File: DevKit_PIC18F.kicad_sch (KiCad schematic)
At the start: 29 parts, among them J1 PIC_ICSP_ICD, J2 USB_B, J3 5P_UART, J4 RA_PORT, J5 RB_PORT, J6 RD_PORT, J7 RC_PORT, J8 RE_PORT, SW1 SW_RST, X1 16MHz

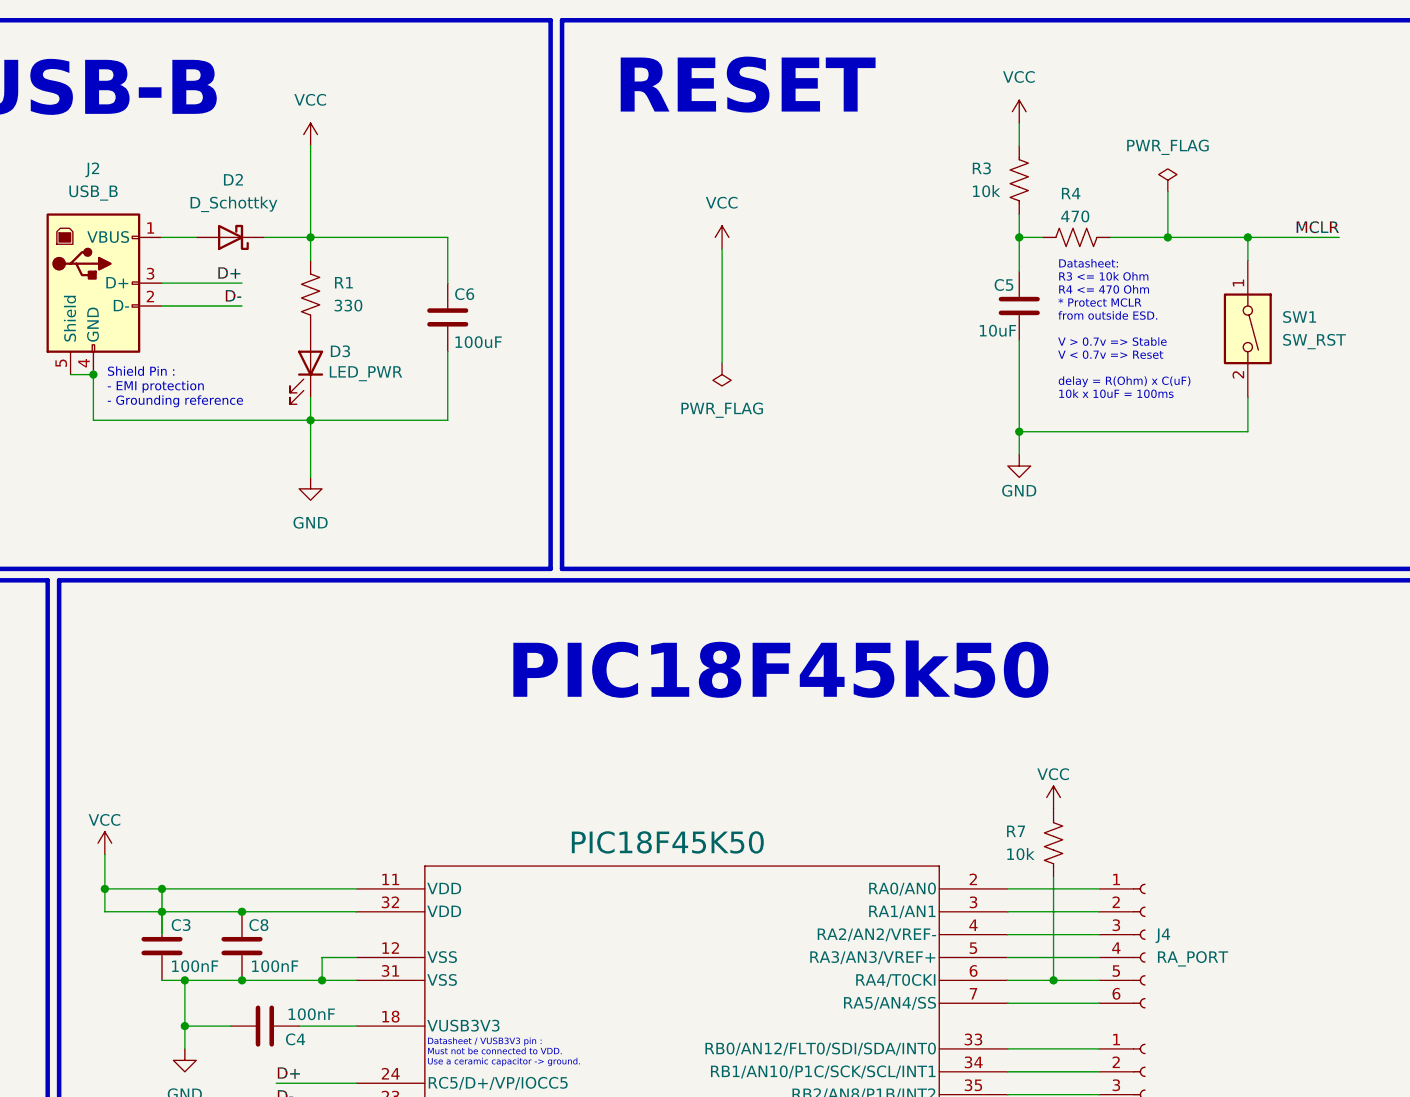
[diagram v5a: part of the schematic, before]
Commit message: Fix PWR_Flag & GND on PCB
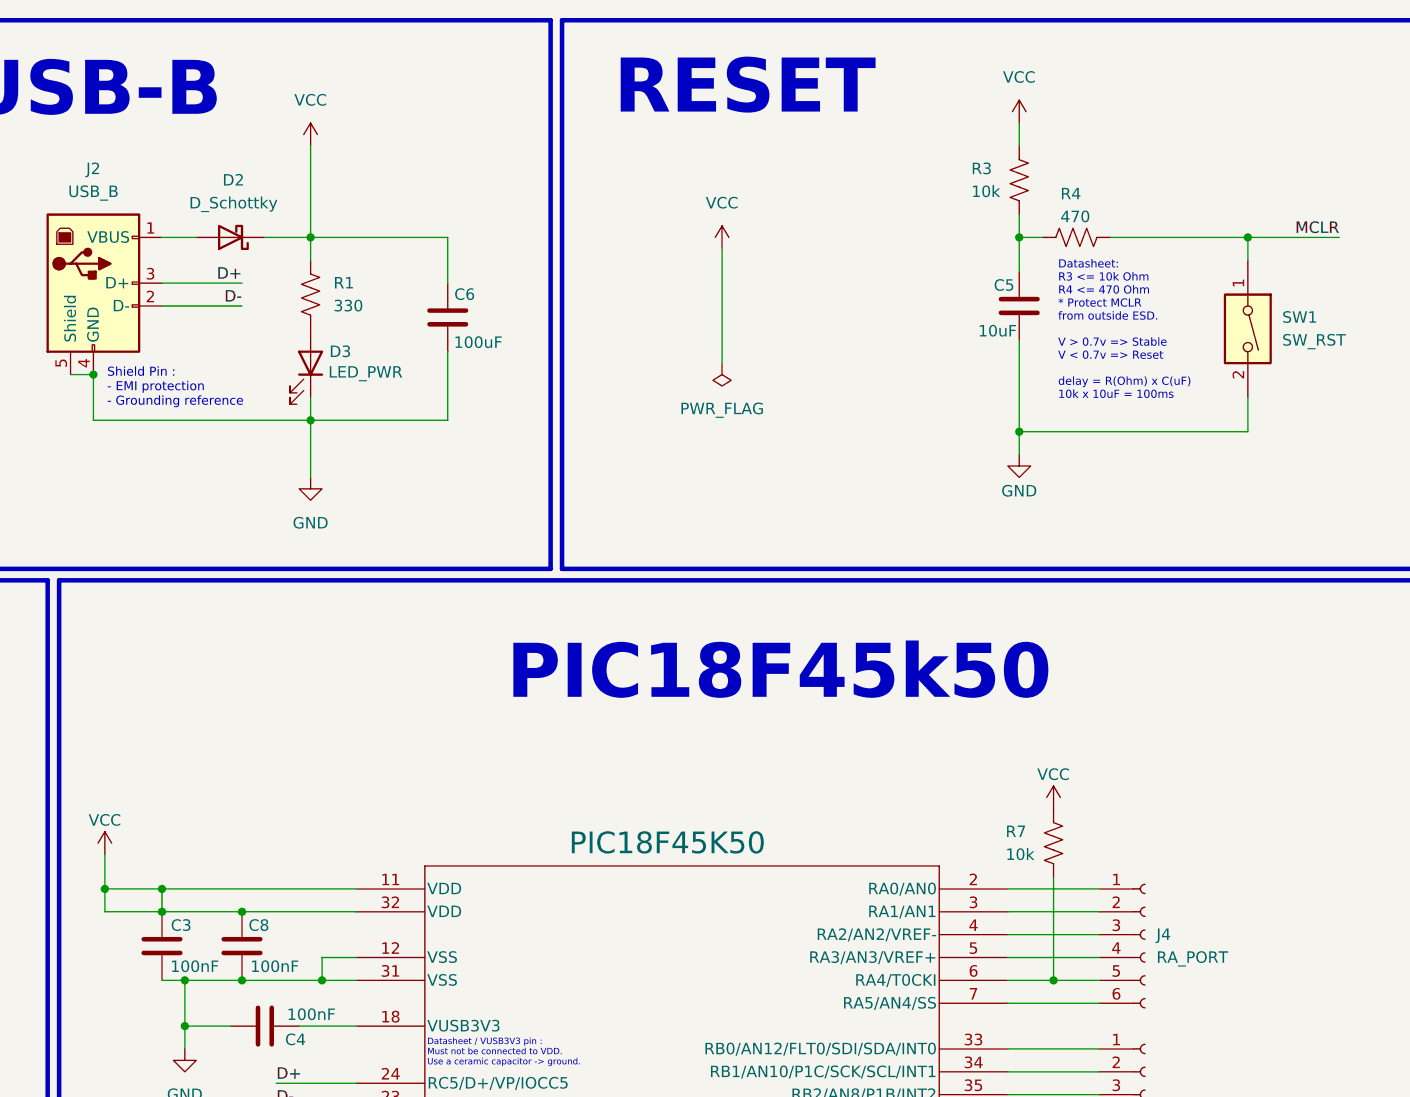
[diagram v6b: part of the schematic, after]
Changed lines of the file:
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@@
 					)
 				)
-				(pin power_in line
+				(pin input line
 					(at 0 -39.37 0)
 					(length 7.62)
@@
 	)
 	(junction
-		(at 210.82 36.83)
-		(diameter 0)
-		(color 0 0 0 0)
-	)
-	(junction
 		(at 194.31 58.42)
 		(diameter 0)
@@
 	(wire
 		(pts
-			(xy 210.82 36.83) (xy 219.71 36.83)
-		)
-		(stroke
-			(width 0)
-			(type default)
-		)
-	)
-	(wire
-		(pts
 			(xy 203.2 127) (xy 193.04 127)
 		)
@@
 	(wire
 		(pts
-			(xy 204.47 36.83) (xy 210.82 36.83)
+			(xy 204.47 36.83) (xy 219.71 36.83)
 		)
 		(stroke
@@
 	(wire
 		(pts
-			(xy 210.82 31.75) (xy 210.82 36.83)
-		)
-		(stroke
-			(width 0)
-			(type default)
-		)
-	)
-	(wire
-		(pts
 			(xy 111.76 153.67) (xy 120.65 153.67)
 		)
@@
 	(wire
 		(pts
-			(xy 99.06 111.76) (xy 99.06 114.3)
-		)
-		(stroke
-			(width 0)
-			(type default)
-		)
-	)
-	(wire
-		(pts
 			(xy 92.71 109.22) (xy 92.71 111.76)
 		)
@@
 			)
 		)
+		(property "Sim.Pins" "1=K 2=A"
+			(at 115.57 50.8 0)
+			(effects
+				(font
+					(size 1.27 1.27)
+				)
+				(hide yes)
+			)
+		)
 		(pin "1"
 		)
@@
 	)
 	(symbol
-		(lib_id "power:PWR_FLAG")
-		(at 210.82 31.75 0)
-		(unit 1)
-		(exclude_from_sim no)
-		(in_bom yes)
-		(on_board yes)
-		(dnp no)
-		(fields_autoplaced yes)
-		(property "Reference" "#FLG01"
-			(at 210.82 29.845 0)
-			(effects
-				(font
-					(size 1.27 1.27)
-				)
-				(hide yes)
-			)
-		)
-		(property "Value" "PWR_FLAG"
-			(at 210.82 26.67 0)
-			(effects
-				(font
-					(size 1.27 1.27)
-				)
-			)
-		)
-		(property "Footprint" ""
-			(at 210.82 31.75 0)
-			(effects
-				(font
-					(size 1.27 1.27)
-				)
-				(hide yes)
-			)
-		)
-		(property "Datasheet" "~"
-			(at 210.82 31.75 0)
-			(effects
-				(font
-					(size 1.27 1.27)
-				)
-				(hide yes)
-			)
-		)
-		(property "Description" "Special symbol for telling ERC where power comes from"
-			(at 210.82 31.75 0)
-			(effects
-				(font
-					(size 1.27 1.27)
-				)
-				(hide yes)
-			)
-		)
-		(pin "1"
-		)
-		(instances
-			(project "DevKit_PIC18F"
-				(path "/495af0d8-3788-4f6a-8ee9-f4c61668daf8"
-					(reference "#FLG01")
-					(unit 1)
-				)
-			)
-		)
-	)
-	(symbol
 		(lib_id "Device:Crystal")
 		(at 45.72 46.99 90)
@@
 			)
 		)
+		(property "Sim.Pins" "1=K 2=A"
+			(at 228.6 154.94 0)
+			(effects
+				(font
+					(size 1.27 1.27)
+				)
+				(hide yes)
+			)
+		)
 		(pin "1"
 		)
@@
 			(at 52.07 99.06 0)
 			(effects
+				(font
+					(size 1.27 1.27)
+				)
+				(hide yes)
+			)
+		)
+		(property "Sim.Pins" "1=K 2=A"
+			(at 52.07 99.06 0)
+			(effects

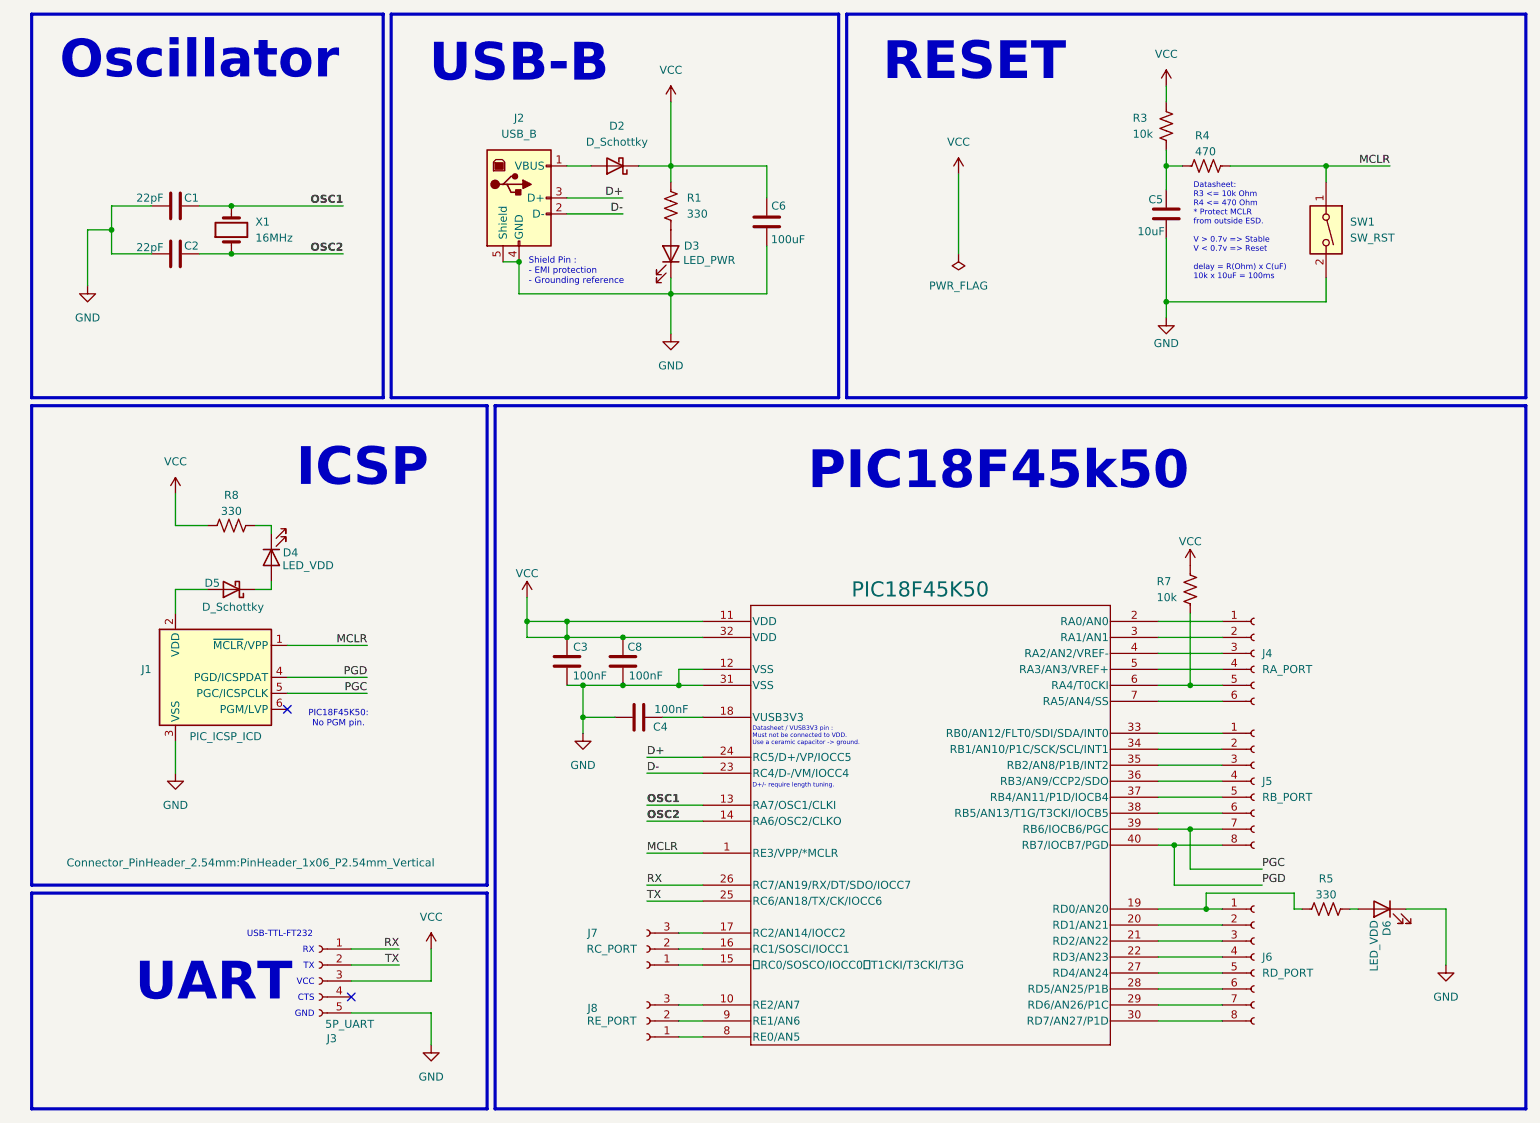
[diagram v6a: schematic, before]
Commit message: Update Rev.8: Fix SCH bug, remove D/R/L from ISCP & D6->RA0
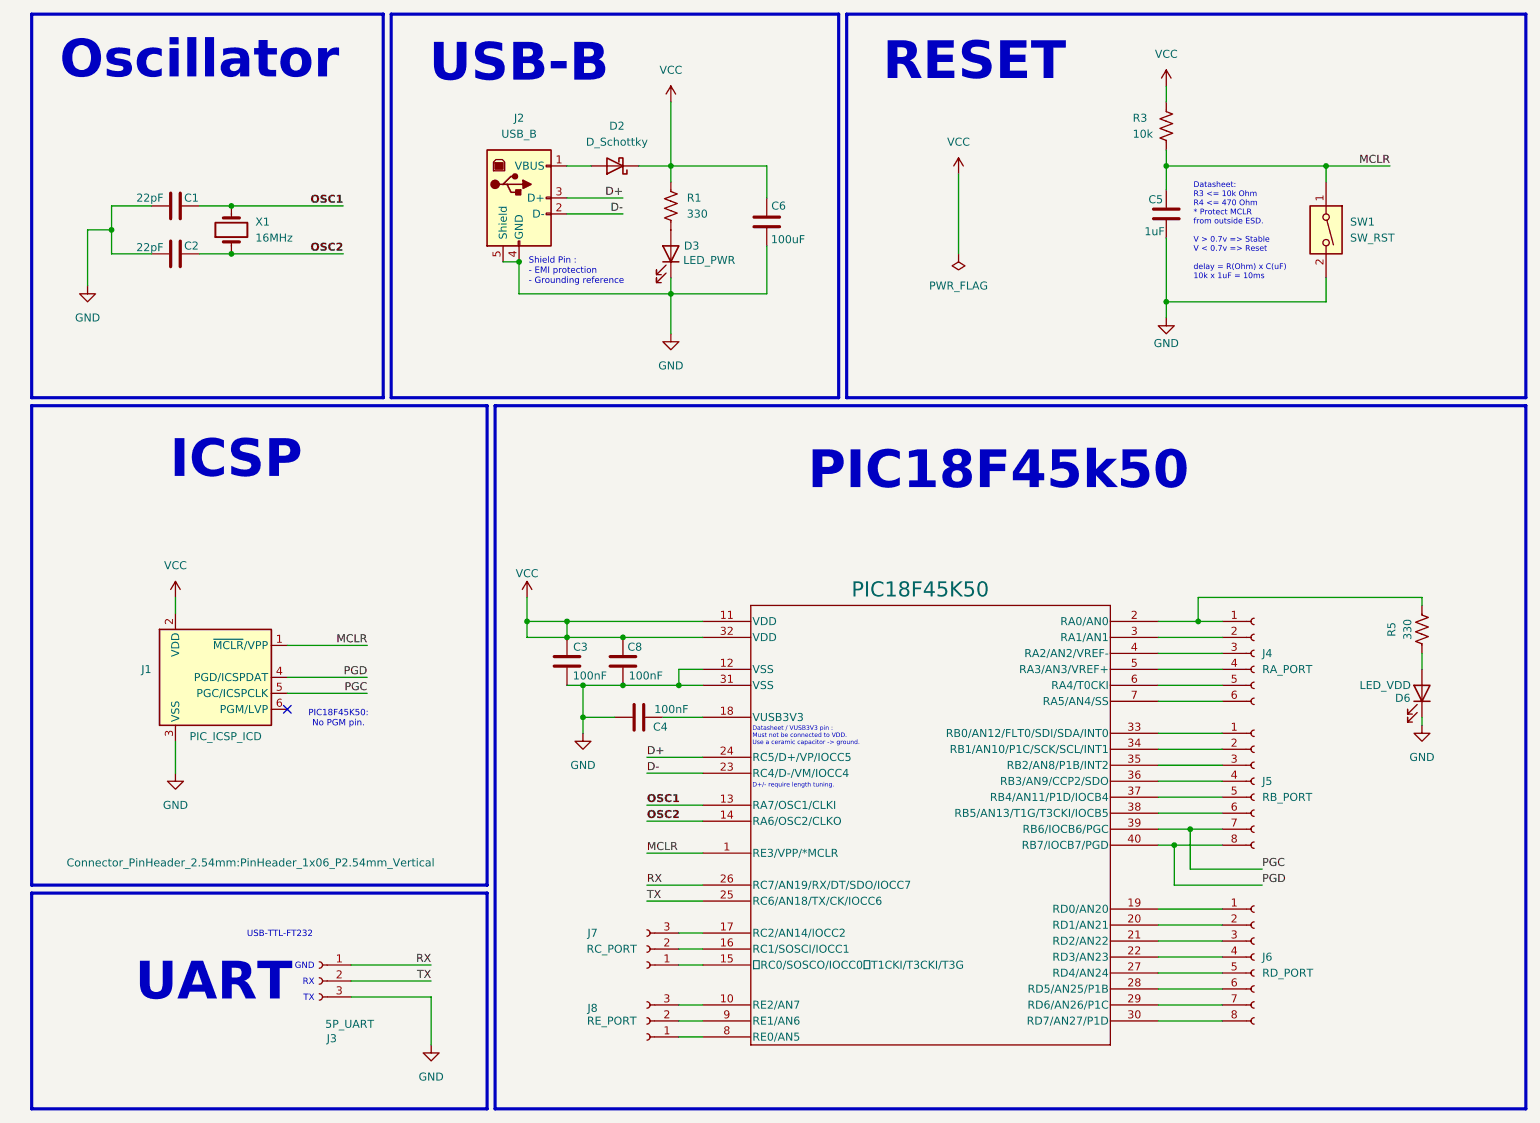
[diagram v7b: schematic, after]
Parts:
- removed D4: LED_VDD, LED_THT:LED_D3.0mm_FlatTop, symbol Device:LED
- removed D5: D_Schottky, Diode_THT:D_DO-34_SOD68_P7.62mm_Horizontal, symbol Device:D_Schottky
- removed R4: 470, Resistor_THT:R_Axial_DIN0204_L3.6mm_D1.6mm_P5.08mm_Horizontal, symbol Device:R_US
- removed R7: 10k, Resistor_THT:R_Axial_DIN0204_L3.6mm_D1.6mm_P5.08mm_Horizontal, symbol Device:R_US
- removed R8: 330, Resistor_THT:R_Axial_DIN0204_L3.6mm_D1.6mm_P5.08mm_Horizontal, symbol Device:R_US
- C5: value 10uF -> 1uF
- J3: footprint Connector_PinSocket_2.54mm:PinSocket_1x05_P2.54mm_Vertical -> Connector_PinSocket_2.54mm:PinSocket_1x03_P2.54mm_Vertical; symbol Connector:Conn_01x05_Socket -> Connector:Conn_01x03_Socket
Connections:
- net GND: now also J3.3 (Pin_3); no longer J3.5 (Pin_5)
- net MCLR: now also C5.2, R3.2
- net VCC: now also J1.2 (VDD); no longer J3.3 (Pin_3)
- net at J6.1 (Pin_1), PIC18F45K50.19 (RD0/AN20): no longer R5.1
- net at D6.2 (A): now also R5.1; no longer R5.2
- net at J4.1 (Pin_1), PIC18F45K50.2 (RA0/AN0): now also R5.2
- no-connect marks 2 -> 1
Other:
- note added: "Datasheet: R3 <= 10k Ohm R4 <= 470 Ohm * Protect MCLR from outside ESD. V > 0.7v => Stable V < 0.7v => Reset delay = R(Ohm) x C(uF) 10k x 1uF = 10ms"
- note removed: "CTS"
- note removed: "Datasheet: R3 <= 10k Ohm R4 <= 470 Ohm * Protect MCLR from outside ESD. V > 0.7v => Stable V < 0.7v => Reset delay = R(Ohm) x C(uF) 10k x 10uF = 100ms"
- note removed: "VCC"
- moved on the sheet: D6, R5
